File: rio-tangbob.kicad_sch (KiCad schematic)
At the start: 66 parts, among them J5 Conn_01x03, J6 Conn_01x03, U1 Tang_Nano_9k, U2 WIZ850io, U3 TXS0108EPW, U4 TXS0108EPW, U5 TXS0108EPW, U6 TXS0108EPW, U7 TXS0108EPW, U8 MAX485E

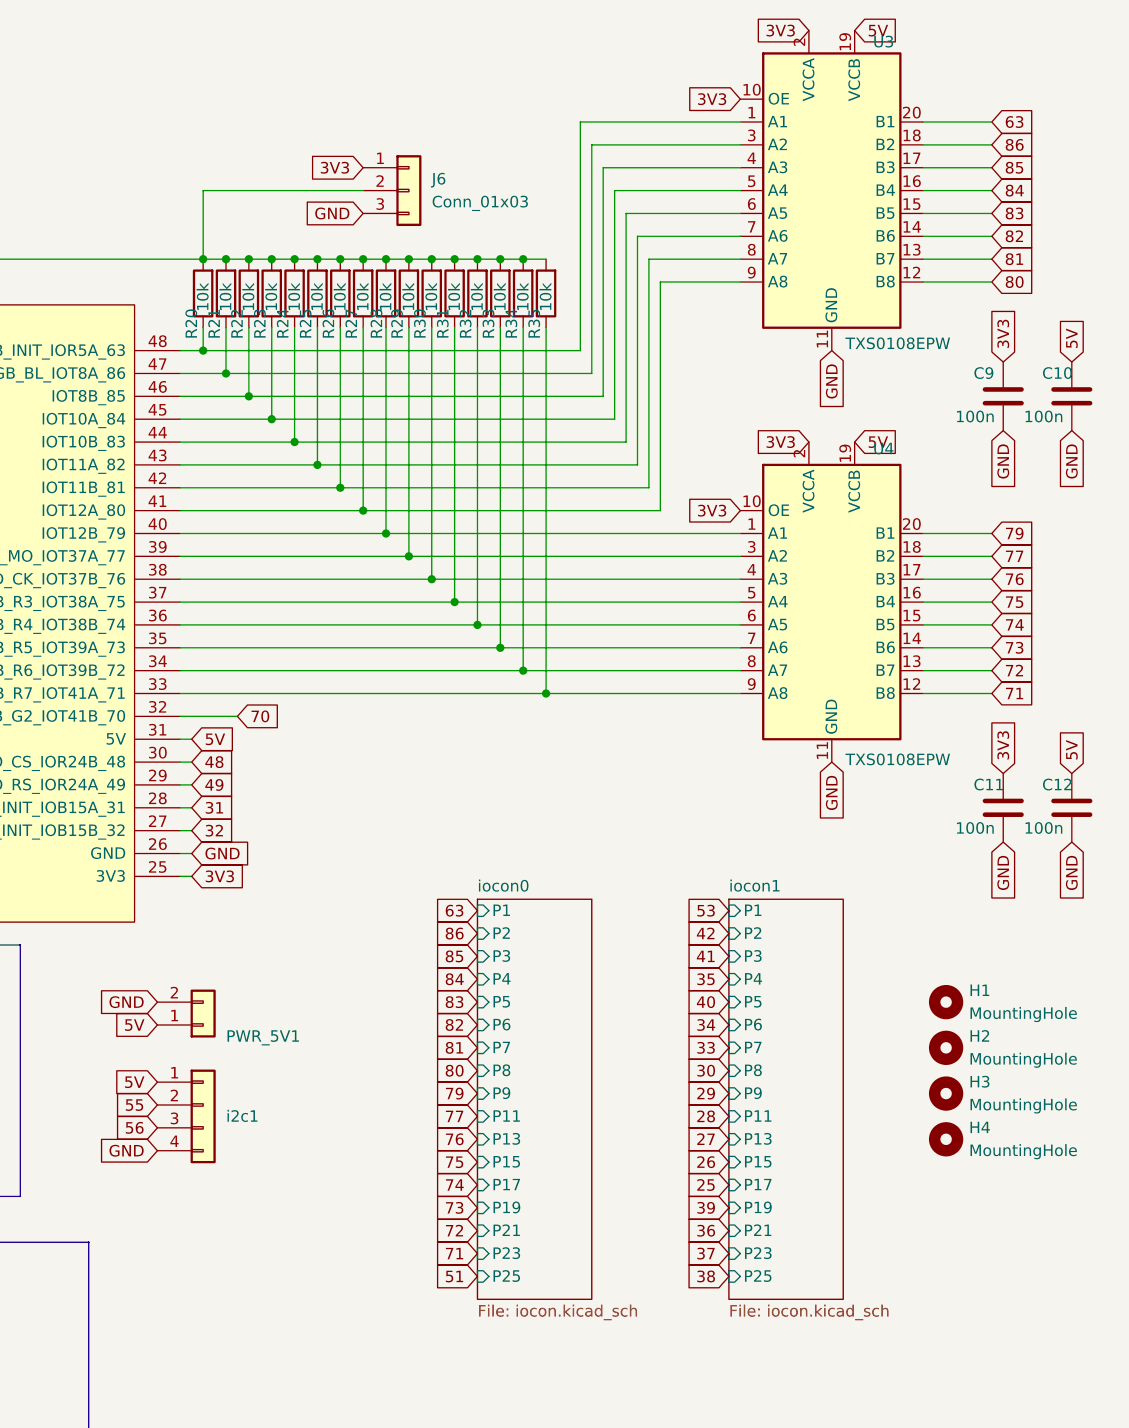
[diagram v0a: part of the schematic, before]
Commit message: set U3+U4 voltage to ~2.7V
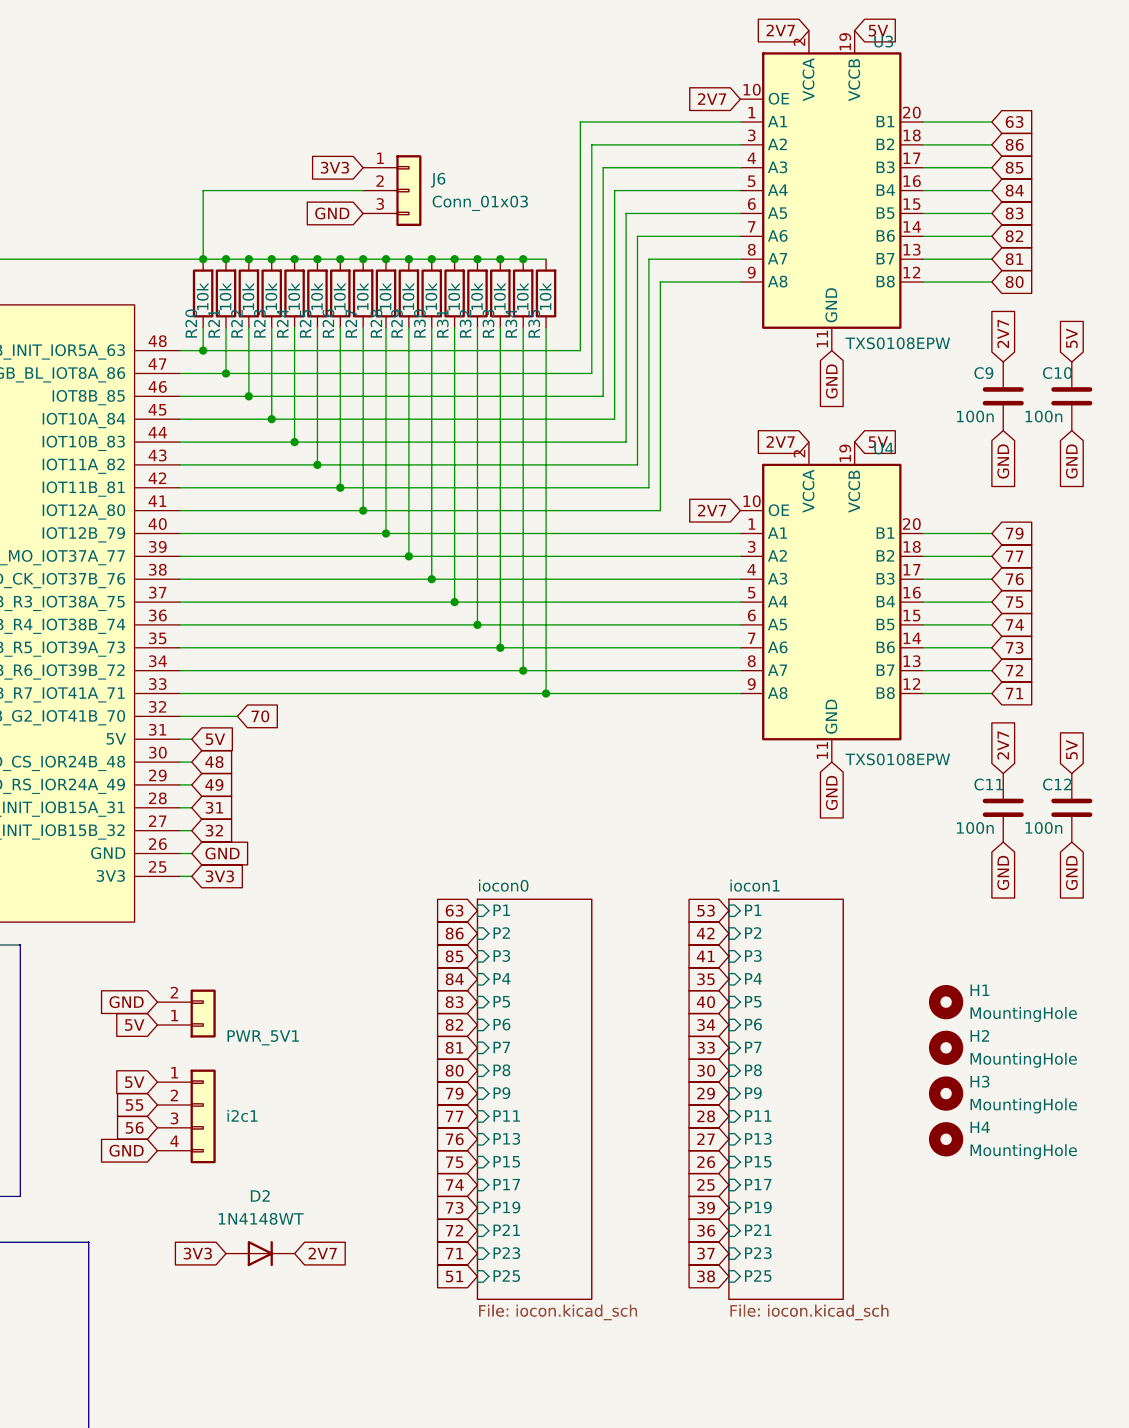
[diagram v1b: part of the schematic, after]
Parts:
- added D2: 1N4148WT, Diode_SMD:D_SOD-523, symbol Diode:1N4148WT
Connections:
- net 3V3: now also D2.2 (A); no longer C11.1, C9.1, U3.10 (OE), U3.2 (VCCA), U4.10 (OE), U4.2 (VCCA)
- new net 2V7: C11.1, C9.1, D2.1 (K), U3.10 (OE), U3.2 (VCCA), U4.10 (OE), U4.2 (VCCA)
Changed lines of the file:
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@@
 		)
 	)
-	(global_label "3V3"
+	(global_label "2V7"
 		(shape input)
 		(at 252.73 62.23 180)
@@
 		)
 	)
-	(global_label "3V3"
+	(global_label "2V7"
 		(shape input)
 		(at 252.73 16.51 180)
@@
 		)
 	)
-	(global_label "3V3"
+	(global_label "2V7"
 		(shape input)
 		(at 274.32 99.06 90)
@@
 		)
 	)
-	(global_label "3V3"
+	(global_label "2V7"
 		(shape input)
 		(at 274.32 53.34 90)
@@
 		)
 	)
+	(global_label "2V7"
+		(shape input)
+		(at 195.58 152.4 0)
+		(fields_autoplaced yes)
+		(effects
+			(font
+				(size 1.27 1.27)
+			)
+			(justify left)
+		)
+		(property "Intersheetrefs" "${INTERSHEET_REFS}"
+			(at 202.0728 152.4 0)
+			(effects
+				(font
+					(size 1.27 1.27)
+				)
+				(justify left)
+				(hide yes)
+			)
+		)
+	)
 	(global_label "41"
 		(shape input)
@@
 		)
 	)
-	(global_label "3V3"
+	(global_label "2V7"
 		(shape input)
 		(at 245.11 24.13 180)
@@
 		)
 	)
+	(global_label "3V3"
+		(shape input)
+		(at 187.96 152.4 180)
+		(fields_autoplaced yes)
+		(effects
+			(font
+				(size 1.27 1.27)
+			)
+			(justify right)
+		)
+		(property "Intersheetrefs" "${INTERSHEET_REFS}"
+			(at 181.4672 152.4 0)
+			(effects
+				(font
+					(size 1.27 1.27)
+				)
+				(justify right)
+				(hide yes)
+			)
+		)
+	)
 	(global_label "53"
 		(shape input)
@@
 		)
 	)
-	(global_label "3V3"
+	(global_label "2V7"
 		(shape input)
 		(at 245.11 69.85 180)
@@
 					(unit 1)
 				)
+			)
+		)
+	)
+	(symbol
+		(lib_id "Diode:1N4148WT")
+		(at 191.77 152.4 180)
+		(unit 1)
+		(exclude_from_sim no)
+		(in_bom yes)
+		(on_board yes)
+		(dnp no)
+		(fields_autoplaced yes)
+		(property "Reference" "D2"
+			(at 191.77 146.05 0)
+			(effects
+				(font
+					(size 1.27 1.27)
+				)
+			)
+		)
+		(property "Value" "1N4148WT"
+			(at 191.77 148.59 0)
+			(effects
+				(font
+					(size 1.27 1.27)
+				)
+			)
+		)
+		(property "Footprint" "Diode_SMD:D_SOD-523"
+			(at 191.77 147.955 0)
+			(effects
+				(font
+					(size 1.27 1.27)
+				)
+				(hide yes)
+			)
+		)
+		(property "Datasheet" "https://www.diodes.com/assets/Datasheets/ds30396.pdf"
+			(at 191.77 152.4 0)
+			(effects
+				(font
+					(size 1.27 1.27)
+				)
+				(hide yes)
+			)
+		)
+		(property "Description" "75V 0.15A Fast switching Diode, SOD-523"
+			(at 191.77 152.4 0)
+			(effects
+				(font
+					(size 1.27 1.27)
+				)
+				(hide yes)
+			)
+		)
+		(property "Sim.Device" "D"
+			(at 191.77 152.4 0)
+			(effects
+				(font
+					(size 1.27 1.27)
+				)
+				(hide yes)
+			)
+		)
+		(property "Sim.Pins" "1=K 2=A"
+			(at 191.77 152.4 0)
+			(effects
+				(font
+					(size 1.27 1.27)
+				)
+				(hide yes)
+			)
+		)
+		(pin "1"
+		)
+		(pin "2"
+		)
+		(instances
+			(project ""
+				(path "/eda038a5-065b-41d3-af81-2fda0f336b09"
+					(reference "D2")
+					(unit 1)
+				)
